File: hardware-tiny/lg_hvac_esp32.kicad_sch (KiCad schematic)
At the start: 15 parts, among them J1 JST_XH_S3B-XH-A-1_01x03, J2 Conn_01x19_Female_1_to_19, J3 Conn_01x19_Female_20_to_38, U1 TPS82130, U2 TJA1027

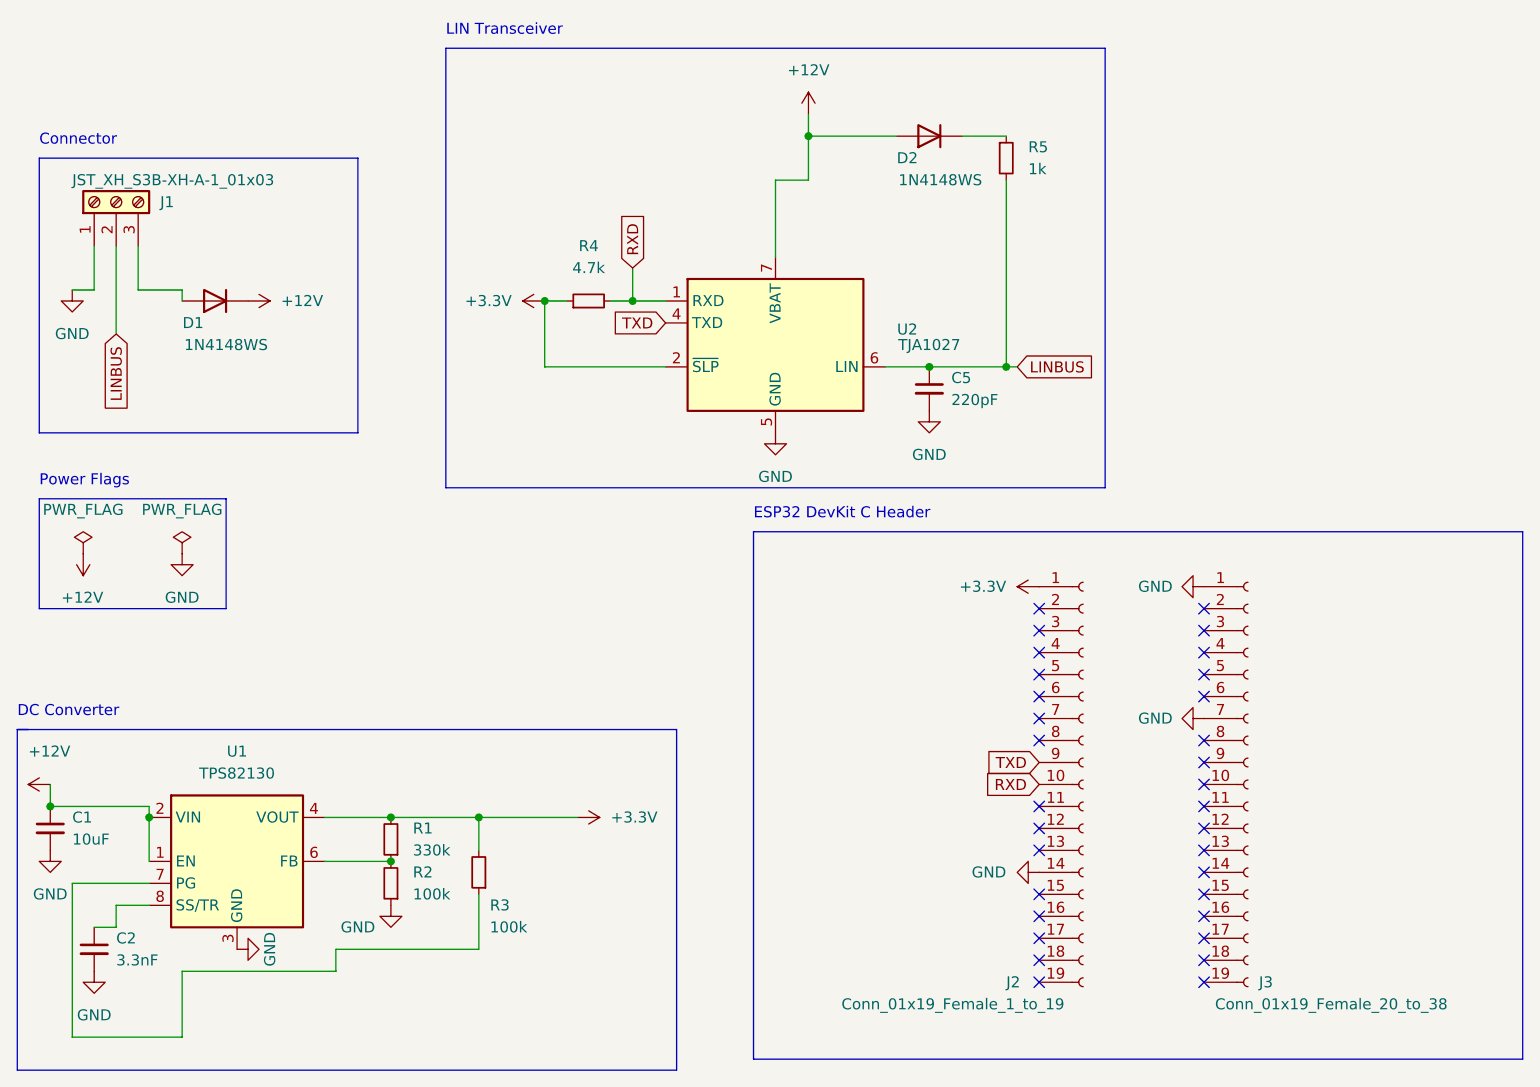
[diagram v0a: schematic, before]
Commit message: Replaced C1 with a component that is available at jlcpcb.
Fixed all DRC errors and warnings.

Updated project files for KiCAD 9. I used the
https://github.com/Bouni/kicad-jlcpcb-tools plugin with some custom
rotation settings for J1, J2, and J3 because the KiCAD library and
jlcpcb disagree.
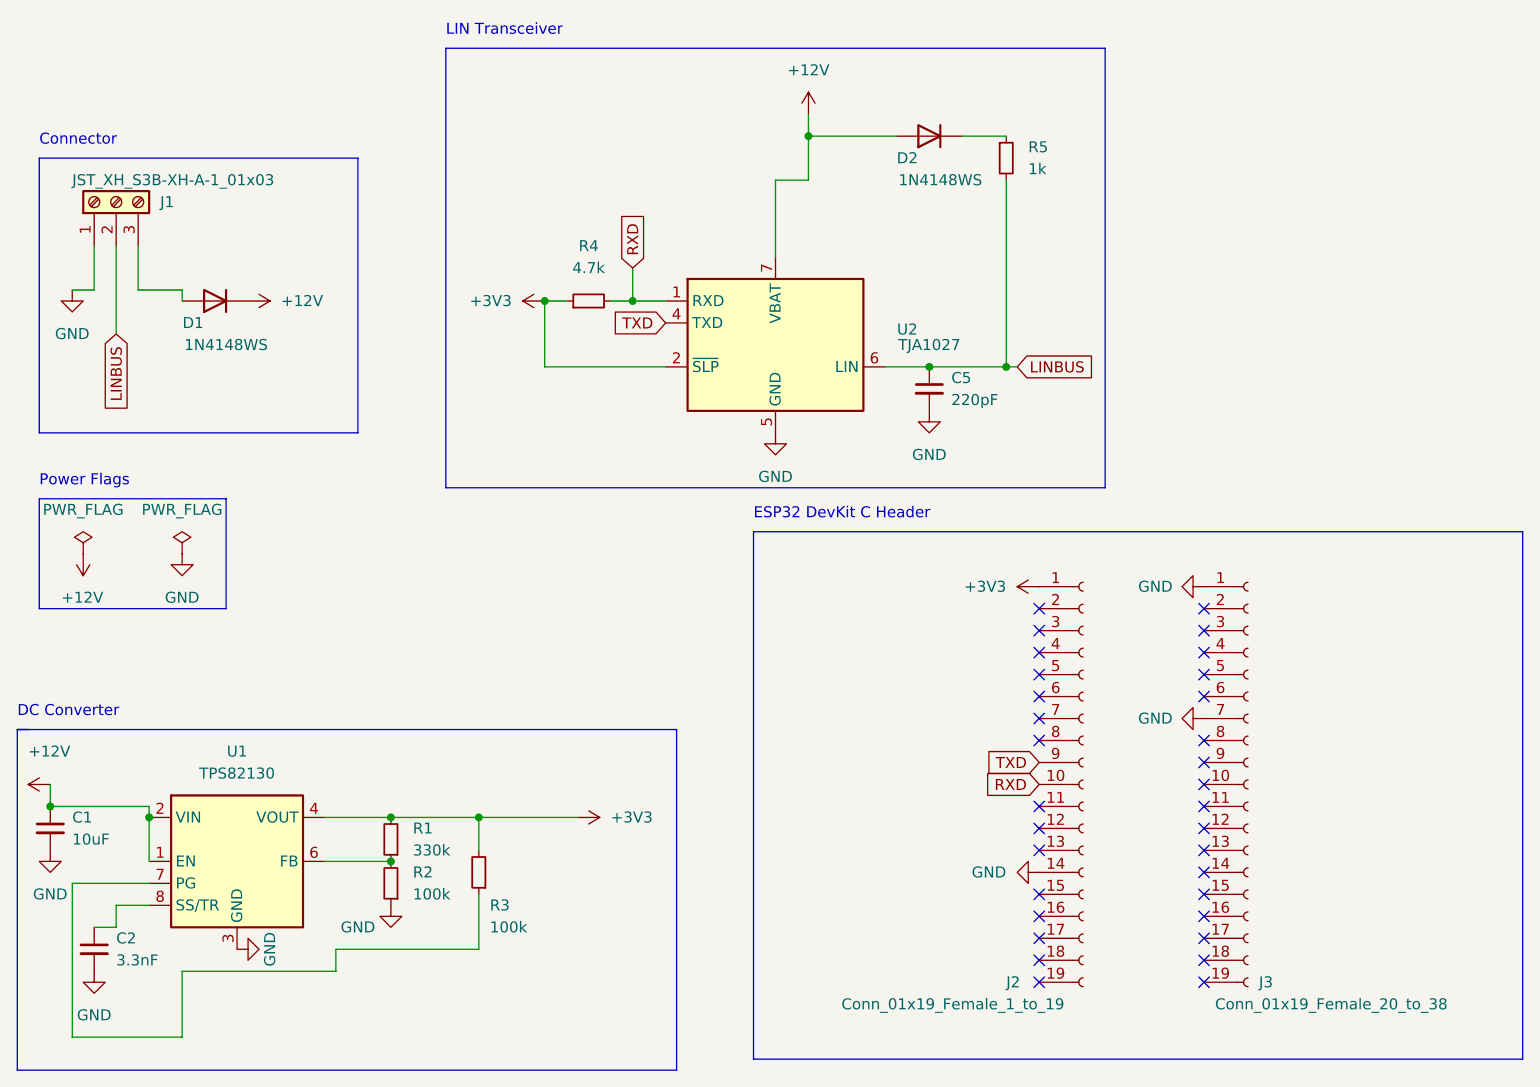
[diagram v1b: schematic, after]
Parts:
- C1: footprint Capacitor_SMD:CP_Elec_4x5.4 -> Capacitor_SMD:C_1210_3225Metric; LCSC C401619 -> C92834
- U1: footprint Package_LGA:Texas_MicroSiP-8-1EP_2.8x3.0mm_P0.65mm_EP1.1x1.9mm_SMD_ThermalVias -> Package_LGA:Texas_SIL0008D_MicroSiP-8-1EP_2.8x3mm_P0.65mm_EP1.1x1.9mm_ThermalVias
- U2: footprint Package_SO:SO-8_3.9x4.9mm_P1.27mm -> Package_SO:SOIC-8_3.9x4.9mm_P1.27mm
